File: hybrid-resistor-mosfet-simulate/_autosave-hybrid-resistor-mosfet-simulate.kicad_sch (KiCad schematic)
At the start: 11 parts, among them Q1 NMOS, U2 ${SIM.PARAMS}

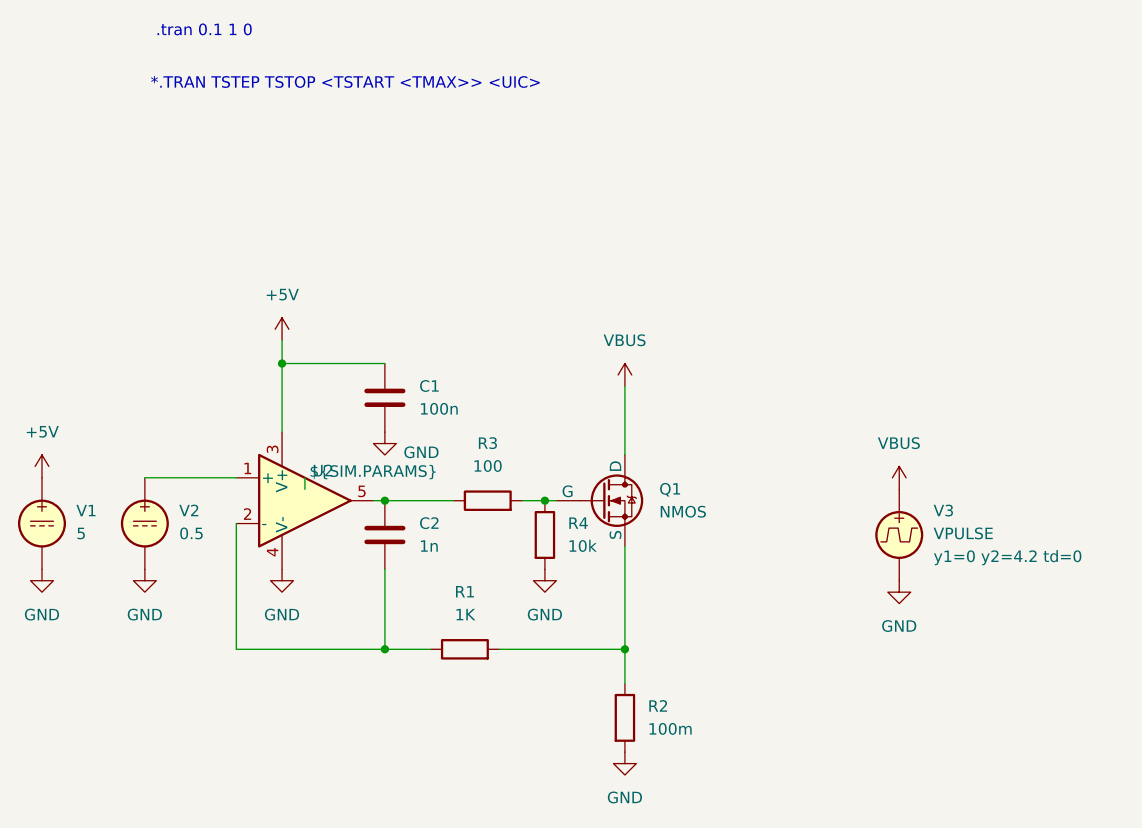
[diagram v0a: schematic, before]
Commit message: First L-C simulation try
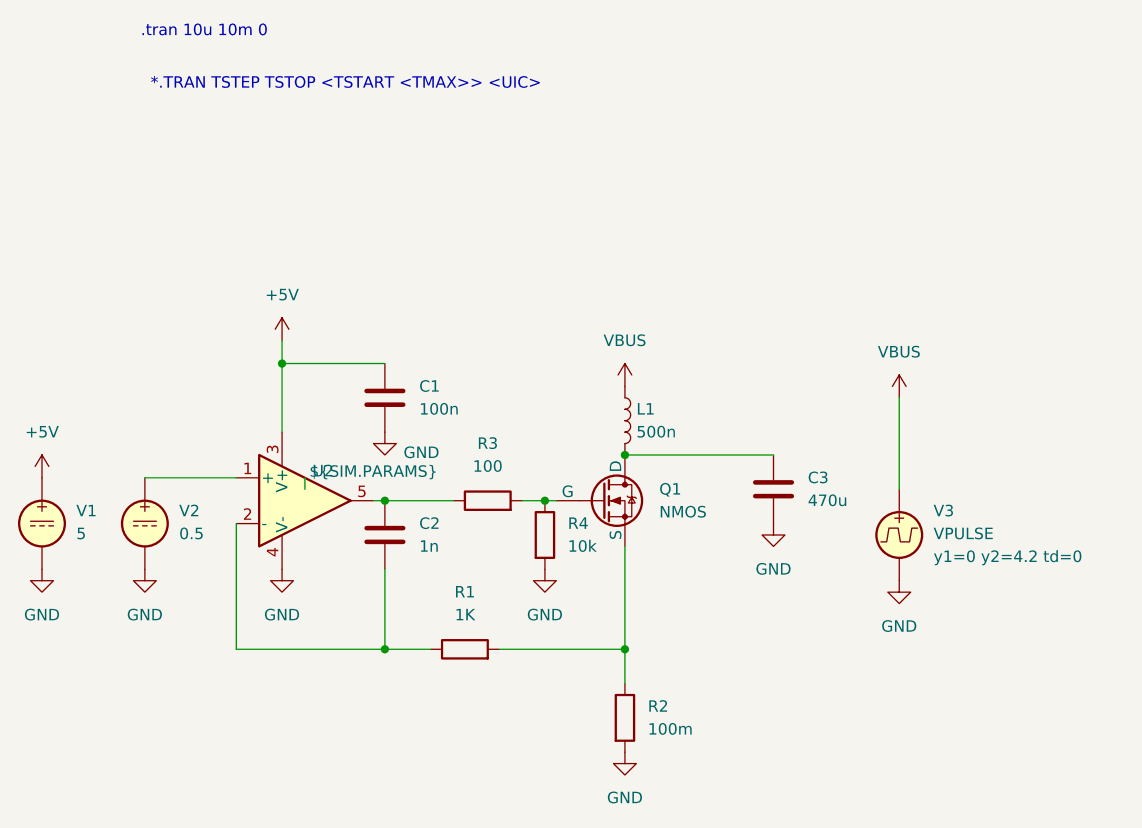
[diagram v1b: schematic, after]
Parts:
- added C3: 470u, symbol Device:C
- added L1: 500n, symbol Device:L
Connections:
- net GND: now also C3.2
- net VBUS: now also L1.1; no longer Q1.1 (D)
- new net: C3.1, L1.2, Q1.1 (D)
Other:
- note added: ".tran 10u 10m 0"
- note removed: ".tran 0.1 1 0"
